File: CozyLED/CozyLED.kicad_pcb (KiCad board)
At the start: 4 copper layers, 100 x 50 mm, 26 parts, among them J1 Barrel_Jack, J2 LCD DISPLAY, J3 LED Pins, J4 UART, Q1 AO3400A, Q2 AO3400A, Q3 AO3400A, SW1 LEFT, SW2 RIGHT, SW3 EN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

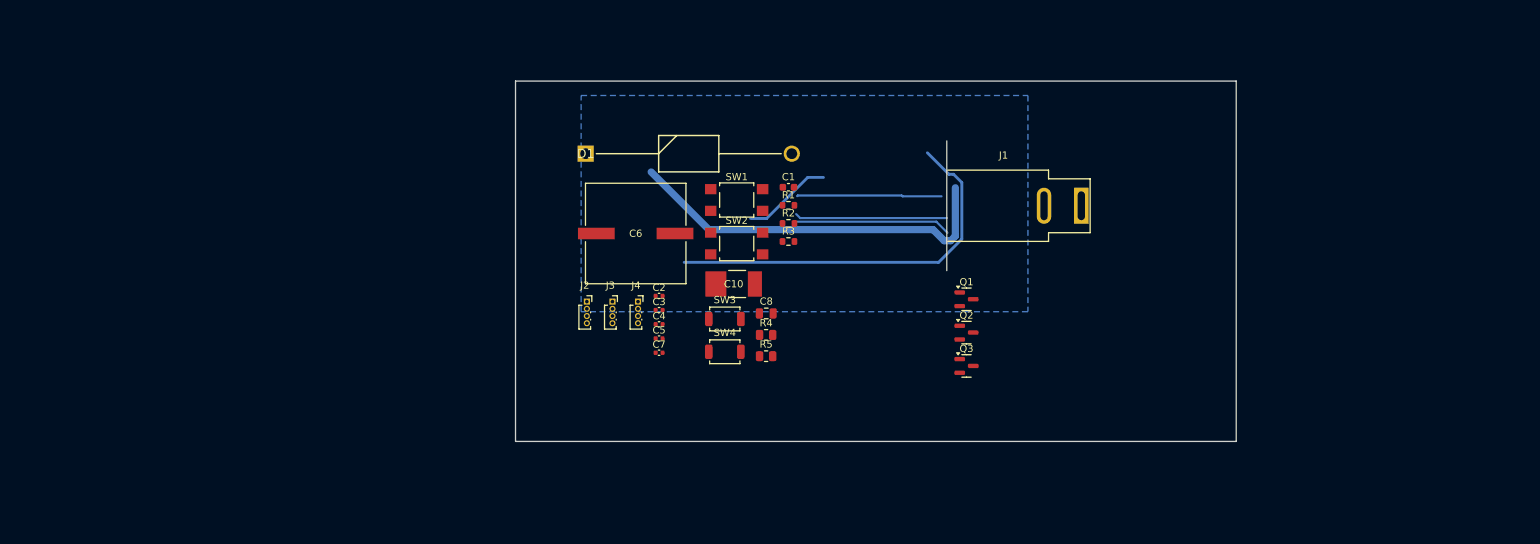
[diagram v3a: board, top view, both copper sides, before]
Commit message: Updated CozyLED PCB
Updates:
- Finalized initial revision of schematic (footprints)
- Initial placement of components in layout
- Initial board margins
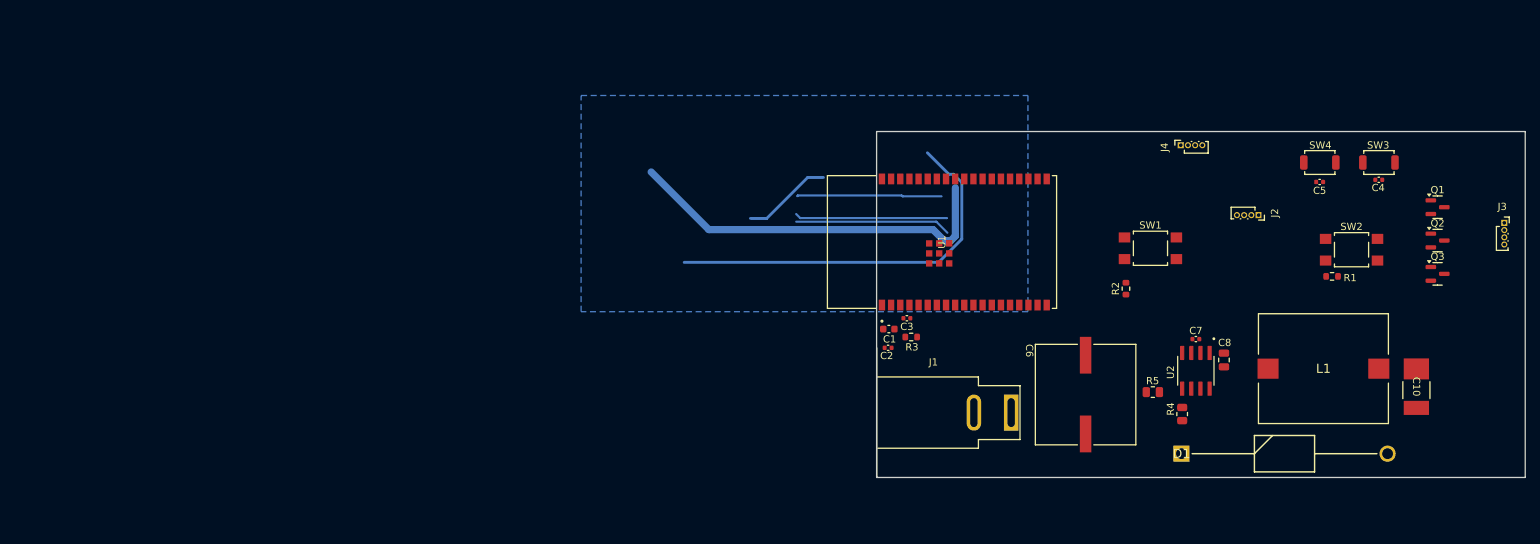
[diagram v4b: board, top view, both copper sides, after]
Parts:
- added L1: DO5022P-154MLD, Inductor:DO5022P154MLD, F.Cu at (162.0, 99.9)
- added U1: ESP32-WROVER-E-N16R8, esp:ESP32-WROVER-E_EXP, F.Cu at (109.1, 82.3)
- added U2: MAX5033AASA_T, Reg_Switch:SOIC127P600X175-8N, F.Cu at (144.3, 100.2)
- C6: value 47u, EEVFK2A470Q -> 47u
- moved J3 124.2 mm to (187.1, 79.7)
- moved C4 101.9 mm to (169.7, 73.7)
- moved C10 95.8 mm to (174.9, 102.4), turned to -90 degrees
- moved C5 94.2 mm to (161.5, 74.0)
- moved J2 94.0 mm to (153.0, 78.6), turned to -90 degrees
- moved SW3 93.3 mm to (169.7, 71.3), turned to 180 degrees
- moved D1 92.6 mm to (142.3, 111.7)
- moved SW4 86.6 mm to (161.5, 71.3), turned to 180 degrees
- moved SW2 85.3 mm to (165.9, 83.4)
- moved J4 78.4 mm to (142.2, 68.9), turned to 90 degrees
- moved R1 76.1 mm to (163.2, 87.1)
- moved C7 74.5 mm to (144.3, 95.8)
- moved Q1 66.6 mm to (177.8, 77.5)
- moved Q2 66.6 mm to (177.8, 82.1)
- moved Q3 66.6 mm to (177.8, 86.8)
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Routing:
- net (no net): track 182.7 -> 75.4 mm
- net GND: track 0.00 -> 107.3 mm
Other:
- board size 100 x 50 mm -> 90 x 48 mm

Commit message: Updated CozyLED schematic and PCB
Updates
- Changed version from Rev B to Rev 1.0
- Revised board to be longer and thinner, since it looked ugly as heck
- Added a missing transistor for the power control on the LED output because I'm dumb as shit and forgot to add one
- Added some nice text to the silkscreen so people know what the name is
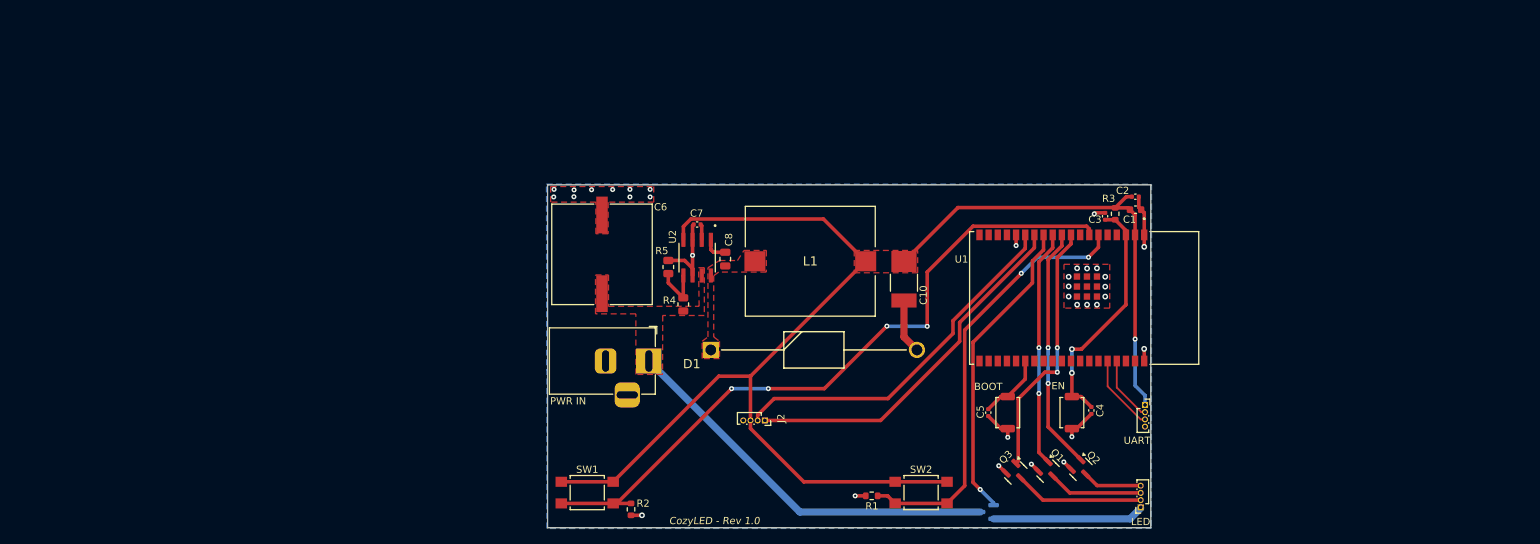
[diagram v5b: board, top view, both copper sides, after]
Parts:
- removed J1: Barrel_Jack, Connector_BarrelJack:BarrelJack_SwitchcraftConxall_RAPC10U_Horizontal
- removed J3: LED Pins, Connector_PinSocket_1.00mm:PinSocket_1x04_P1.00mm_Vertical
- removed J4: UART, Connector_PinSocket_1.00mm:PinSocket_1x04_P1.00mm_Vertical
- removed SW3: EN, Button_Switch_SMD:SW_SPST_TS-1088-xR020
- removed SW4: BOOT, Button_Switch_SMD:SW_SPST_TS-1088-xR020
- added BOOT: BOOT, Button_Switch_SMD:SW_SPST_TS-1088-xR020, F.Cu at (118.2, 106.0)
- added EN: EN, Button_Switch_SMD:SW_SPST_TS-1088-xR020, F.Cu at (127.1, 106.0)
- added LED: LED Pins, Connector_PinSocket_1.00mm:PinSocket_1x04_P1.00mm_Vertical, F.Cu at (136.6, 119.1)
- added PWR IN: Barrel_Jack_Switch, Connector_BarrelJack:BarrelJack_Horizontal, F.Cu at (68.4, 98.8)
- added Q4: AO3400A, Package_TO_SOT_SMD:SOT-23, B.Cu at (115.3, 119.8)
- added UART: UART, Connector_PinSocket_1.00mm:PinSocket_1x04_P1.00mm_Vertical, F.Cu at (137.2, 104.9)
- moved SW1 85.2 mm to (59.9, 117.1)
- moved R2 75.2 mm to (65.9, 119.4), turned to -90 degrees
- moved J2 74.2 mm to (84.5, 107.1)
- moved L1 72.7 mm to (90.8, 85.0)
- moved C10 72.6 mm to (103.8, 87.5)
- moved C7 71.0 mm to (75.1, 79.9)
- moved U2 71.0 mm to (75.1, 84.5)
- moved R4 70.9 mm to (73.2, 91.0)
- moved R1 70.8 mm to (99.3, 117.5), turned to 180 degrees
- moved C8 70.6 mm to (79.0, 84.7)
- moved C6 69.9 mm to (61.9, 84.0)
- moved R5 69.4 mm to (71.1, 85.8), turned to 90 degrees
- moved SW2 68.6 mm to (106.2, 117.1)
- moved D1 66.9 mm to (77.0, 97.3)
- moved Q1 65.3 mm to (123.8, 114.1), turned to -45 degrees
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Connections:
- U1 pad 10: /LED_G -> /GPIO_G
- U1 pad 11: /LED_R -> /GPIO_R
- U1 pad 12: /LED_PWR -> /GPIO_PWR
- U1 pad 9: /LED_B -> /GPIO_B
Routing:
- net +3V3: track 0.00 -> 189.1 mm, vias 0 -> 1
- net /LBTN: track 0.00 -> 97.1 mm, vias 0 -> 4
- net (no net): track 75.4 -> 0.00 mm
- net /RBTN: track 0.00 -> 60.2 mm, vias 0 -> 2
- net GND: track 107.3 -> 48.2 mm, vias 0 -> 34
- net +12V: track 0.00 -> 54.6 mm
- net /SDA: track 0.00 -> 50.6 mm
- net /SCL: track 0.00 -> 50.4 mm
- net /GPIO_PWR: track 0.00 -> 42.7 mm, vias 0 -> 1
- net /GPIO_B: track 0.00 -> 35.9 mm, vias 0 -> 2
- net /GPIO_G: track 0.00 -> 33.9 mm, vias 0 -> 2
- net /EN: track 0.00 -> 33.7 mm, vias 0 -> 2
- net /GPIO_R: track 0.00 -> 32.8 mm, vias 0 -> 2
- net /LED_PWR: track 0.00 -> 21.0 mm
- net /LED_B: track 0.00 -> 17.9 mm
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- added copper zone on F.Cu, net +12V
- added copper zone on F.Cu, net +3V3
- added copper zone on B.Cu, net GND
- added copper zone on F.Cu, net GND
- added copper zone on F.Cu, net Net-(D1-K)
- removed copper zone on B.Cu, net (none)
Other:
- board size 90 x 48 mm -> 83.7 x 47.6 mm
- copper layers 4 -> 2
- board text added: "CozyLED - Rev 1.0"
